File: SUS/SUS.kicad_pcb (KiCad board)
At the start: 4 copper layers, 117.7 x 30.4 mm, 69 parts, among them J1 ESP32_Connector_0, J2 ESP32_Connector_1, J3 I2C, J4 I2C, J5 I2C, J6 ADC, J7 WS, U1 TJA1051T, U2 ADS8320EB_250, U3 ICM-42688-P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

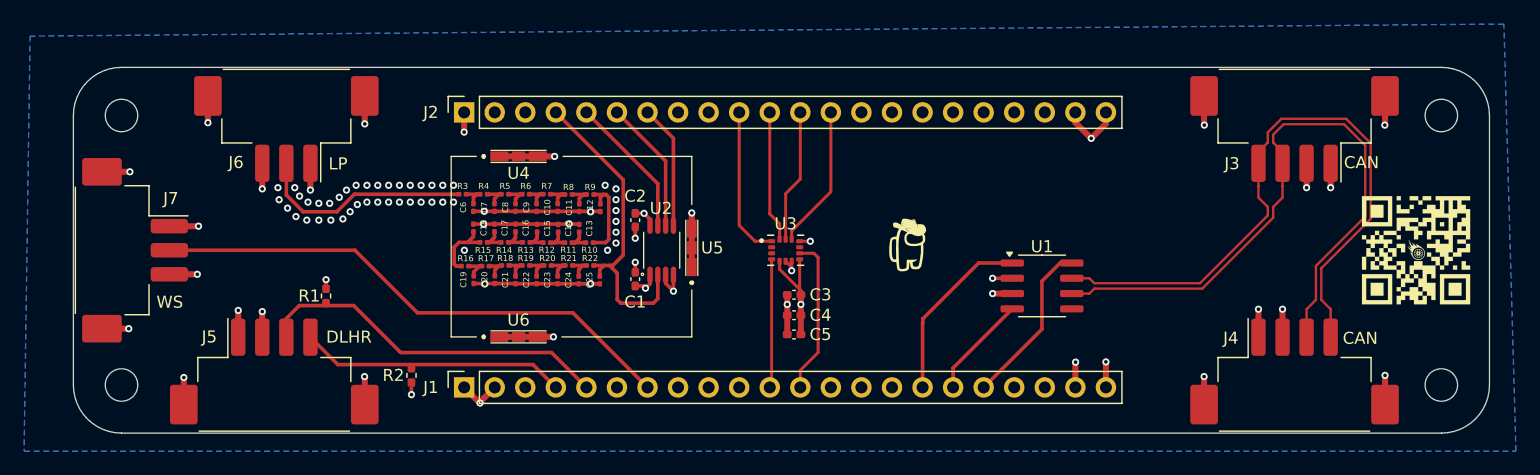
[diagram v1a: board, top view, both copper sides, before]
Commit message: added pads to connect 3.3v or 5v to lin pots & other last minute changes
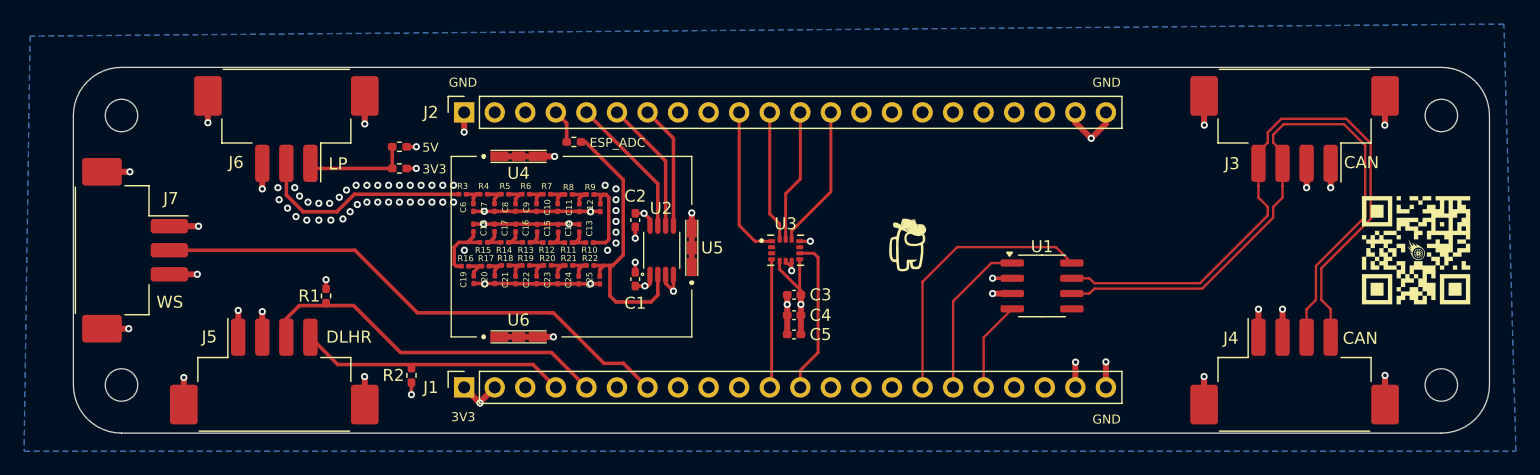
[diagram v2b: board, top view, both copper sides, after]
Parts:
- added R23: 0, Resistor_SMD:R_0402_1005Metric_Pad0.72x0.64mm_HandSolder, F.Cu at (64.4, 53.2)
- added R24: 0, Resistor_SMD:R_0402_1005Metric_Pad0.72x0.64mm_HandSolder, F.Cu at (64.4, 51.4)
- added R27: 0, Resistor_SMD:R_0402_1005Metric_Pad0.72x0.64mm_HandSolder, F.Cu at (78.9, 51.0)
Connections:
- net A_SCL renamed A_SCK
- net A_SDA renamed A_MISO
- C1 pad 1: +3.3V -> +5V
- J1 pad 16: CAN_TX -> CAN_S
- J1 pad 17: CAN_RX -> CAN_TX
- J1 pad 18: CAN_S -> CAN_RX
- J2 pad 12: IMU_SCL -> IMU_SCK
- J2 pad 4: AA_out -> Net-(J2-Pin_4)
- J6 pad 1: +5V -> Net-(J6-Pin_1)
- U2 pad 1: +3.3V -> +5V
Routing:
- net CAN_S: track 13.9 -> 22.9 mm
- net Net-(J6-Pin_1): track 0.00 -> 8.78 mm
- net AA_out: track 26.7 -> 23.6 mm
- net Net-(J2-Pin_4): track 0.00 -> 2.83 mm
- net CAN_TX: track 15.1 -> 13.4 mm
- net +3.3V: track 19.0 -> 17.6 mm
- net CAN_RX: track 8.57 -> 7.51 mm
- net +5V: track 15.0 -> 15.6 mm, vias 7 -> 8
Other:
- board text added: "3V3"
- board text added: "5V"
- board text added: "ESP_ADC"
- board text added: "GND"

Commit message: Removed Vias
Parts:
- U3: footprint ICM-42688-P:PQFN50P300X250X97-14N -> IMU:ICM-42688-P
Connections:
- U3 pad 13: IMU_SCL -> IMU_SCK
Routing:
- net IMU_SCL: track 11.1 -> 0.00 mm
- net IMU_SCK: track 0.00 -> 11.1 mm
- net GND: vias 79 -> 71
